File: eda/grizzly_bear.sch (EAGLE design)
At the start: 60 parts, among them Q1 PSMN4R0, Q2 PSMN4R0, Q3 PSMN4R0, Q4 PSMN4R0, Q5 IPD90P03P4L, U1 A4940, U2 ATMEGA32U4-AU, U3 ACS714, U4 UA78L00, U5 ISL83491SOIC, Y1 16MHz

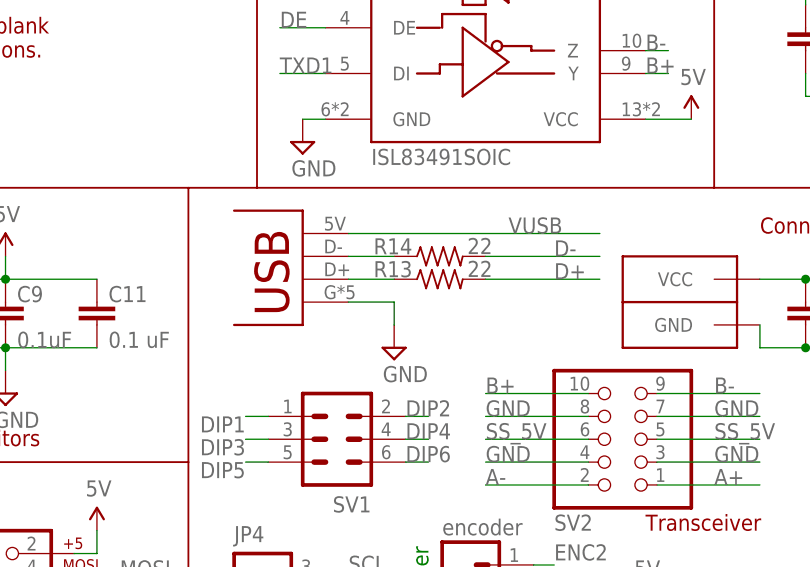
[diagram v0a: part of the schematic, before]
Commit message: Replace USB Mini with USB Micro AB on board, clean up traces and silkscreen
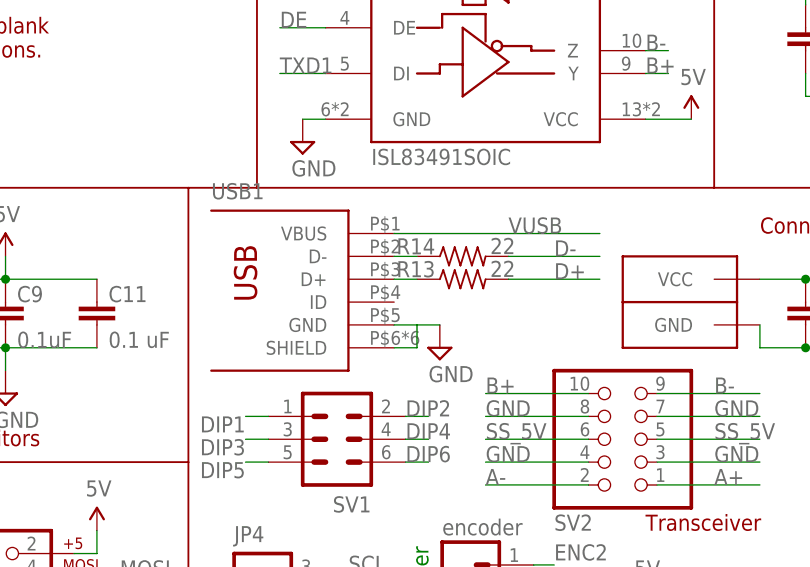
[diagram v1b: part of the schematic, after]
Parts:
- removed U$2: USB-M26FTR, pie:USB-M26FTR
- added USB1: USB-OTGMICRO-AB, pie:USB-OTGMICRO-AB
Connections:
- net D+-_CON: now also USB1.D+; no longer U$2.D+
- net D-_CON: now also USB1.D-; no longer U$2.D-
- net GND: now also USB1.GND, USB1.SHIELD; no longer U$2.G
- net VUSB: now also USB1.VBUS; no longer U$2.5V
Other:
- moved on the sheet: R13, R14
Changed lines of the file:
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@@
 <?xml version="1.0" encoding="utf-8"?>
 <!DOCTYPE eagle SYSTEM "eagle.dtd">
-<eagle version="6.5.0">
+<eagle version="7.4.0">
 <drawing>
 <settings>
@@
 <part name="C4" library="pie" deviceset="CAP" device="1206" value="10uF"/>
 <part name="R1" library="pie" deviceset="R-US_" device="R0603" value="10k"/>
-<part name="U$2" library="pie" deviceset="USB-M26FTR" device=""/>
 <part name="C13" library="pie" deviceset="CAP" device="0603-CAP" value="1uF"/>
 <part name="SUPPLY13" library="pie" deviceset="GND" device=""/>
@@
 <part name="C17" library="pie" deviceset="CAP" device="0603-CAP" value="0.1uF"/>
 <part name="JP1" library="SparkFun-Connectors" deviceset="M02" device="PTH"/>
+<part name="USB1" library="pie" deviceset="USB-OTG" device="MICRO-AB"/>
 </parts>
 <sheets>
@@
 </instance>
 <instance part="R1" gate="G$1" x="205.74" y="43.18" rot="R90"/>
-<instance part="U$2" gate="G$1" x="88.9" y="53.34" rot="R180"/>
 <instance part="C13" gate="G$1" x="15.24" y="119.38" smashed="yes" rot="R270">
 <attribute name="NAME" x="16.51" y="119.38" size="1.778" layer="95"/>
@@
 </instance>
 <instance part="SUPPLY13" gate="GND" x="15.24" y="111.76"/>
-<instance part="R14" gate="G$1" x="109.22" y="50.8" smashed="yes">
-<attribute name="NAME" x="101.854" y="51.0286" size="1.778" layer="95"/>
-<attribute name="VALUE" x="112.268" y="51.054" size="1.778" layer="96"/>
-</instance>
-<instance part="R13" gate="G$1" x="109.22" y="48.26" smashed="yes">
-<attribute name="NAME" x="101.854" y="48.4886" size="1.778" layer="95"/>
-<attribute name="VALUE" x="112.268" y="48.514" size="1.778" layer="96"/>
+<instance part="R14" gate="G$1" x="111.76" y="50.8" smashed="yes">
+<attribute name="NAME" x="104.394" y="51.0286" size="1.778" layer="95"/>
+<attribute name="VALUE" x="114.808" y="51.054" size="1.778" layer="96"/>
+</instance>
+<instance part="R13" gate="G$1" x="111.76" y="48.26" smashed="yes">
+<attribute name="NAME" x="104.394" y="48.4886" size="1.778" layer="95"/>
+<attribute name="VALUE" x="114.808" y="48.514" size="1.778" layer="96"/>
 </instance>
 <instance part="U$3" gate="G$1" x="27.94" y="132.08" smashed="yes">
 <attribute name="VALUE" x="24.384" y="133.096" size="1.778" layer="96"/>
 </instance>
-<instance part="SUPPLY19" gate="GND" x="104.14" y="40.64"/>
+<instance part="SUPPLY19" gate="GND" x="109.22" y="40.64"/>
 <instance part="U$10" gate="G$1" x="5.08" y="33.02"/>
 <instance part="C1" gate="G$1" x="149.86" y="45.72" smashed="yes" rot="R270">
@@
 </instance>
 <instance part="JP1" gate="G$1" x="10.16" y="12.7"/>
+<instance part="USB1" gate="G$1" x="91.44" y="48.26"/>
 </instances>
 <busses>
@@
 <net name="D-" class="0">
 <segment>
-<wire x1="114.3" y1="50.8" x2="127" y2="50.8" width="0.1524" layer="91"/>
+<wire x1="116.84" y1="50.8" x2="127" y2="50.8" width="0.1524" layer="91"/>
 <pinref part="R14" gate="G$1" pin="2"/>
 <label x="121.92" y="50.8" size="1.778" layer="95"/>
@@
 <net name="D+" class="0">
 <segment>
-<wire x1="114.3" y1="48.26" x2="127" y2="48.26" width="0.1524" layer="91"/>
+<wire x1="116.84" y1="48.26" x2="127" y2="48.26" width="0.1524" layer="91"/>
 <pinref part="R13" gate="G$1" pin="2"/>
 <label x="121.92" y="48.26" size="1.778" layer="95"/>
@@
 <net name="D+-_CON" class="0">
 <segment>
-<pinref part="U$2" gate="G$1" pin="D+"/>
-<wire x1="99.06" y1="48.26" x2="104.14" y2="48.26" width="0.1524" layer="91"/>
 <pinref part="R13" gate="G$1" pin="1"/>
+<pinref part="USB1" gate="G$1" pin="D+"/>
+<wire x1="104.14" y1="48.26" x2="106.68" y2="48.26" width="0.1524" layer="91"/>
 </segment>
 </net>
 <net name="D-_CON" class="0">
 <segment>
-<pinref part="U$2" gate="G$1" pin="D-"/>
-<wire x1="99.06" y1="50.8" x2="104.14" y2="50.8" width="0.1524" layer="91"/>
 <pinref part="R14" gate="G$1" pin="1"/>
+<pinref part="USB1" gate="G$1" pin="D-"/>
+<wire x1="104.14" y1="50.8" x2="106.68" y2="50.8" width="0.1524" layer="91"/>
 </segment>
 </net>
 <net name="VUSB" class="0">
 <segment>
-<pinref part="U$2" gate="G$1" pin="5V"/>
 <label x="116.84" y="53.34" size="1.778" layer="95"/>
-<wire x1="127" y1="53.34" x2="99.06" y2="53.34" width="0.1524" layer="91"/>
+<wire x1="127" y1="53.34" x2="104.14" y2="53.34" width="0.1524" layer="91"/>
+<pinref part="USB1" gate="G$1" pin="VBUS"/>
 </segment>
 <segment>
@@
 </segment>
 <segment>
-<pinref part="SUPPLY19" gate="GND" pin="GND"/>
-<wire x1="104.14" y1="43.18" x2="104.14" y2="45.72" width="0.1524" layer="91"/>
-<pinref part="U$2" gate="G$1" pin="G"/>
-<wire x1="99.06" y1="45.72" x2="104.14" y2="45.72" width="0.1524" layer="91"/>
-</segment>
-<segment>
 <wire x1="96.52" y1="10.16" x2="99.06" y2="10.16" width="0.1524" layer="91"/>
 <pinref part="SUPPLY3" gate="GND" pin="GND"/>
@@
 <pinref part="SV2" gate="G$1" pin="8"/>
 </segment>
-</net>
+<segment>
+<pinref part="USB1" gate="G$1" pin="GND"/>
+<pinref part="SUPPLY19" gate="GND" pin="GND"/>
+<wire x1="104.14" y1="43.18" x2="106.68" y2="43.18" width="0.1524" layer="91"/>
+<pinref part="USB1" gate="G$1" pin="SHIELD"/>
+<wire x1="106.68" y1="43.18" x2="109.22" y2="43.18" width="0.1524" layer="91"/>
+<wire x1="104.14" y1="40.64" x2="106.68" y2="40.64" width="0.1524" layer="91"/>
+<wire x1="106.68" y1="40.64" x2="106.68" y2="43.18" width="0.1524" layer="91"/>
+</segment>
+</net>
